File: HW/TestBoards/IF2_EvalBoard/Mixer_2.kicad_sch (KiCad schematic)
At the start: 23 parts, among them IC1 SIM-14+, IC2 LEE2-6+, IC3 LEE2-6+, J1 Conn_01x04, J2 SMA, J3 SMA, J4 SMA, J5 MS-156C3_20_, U1 B39871B4316P810

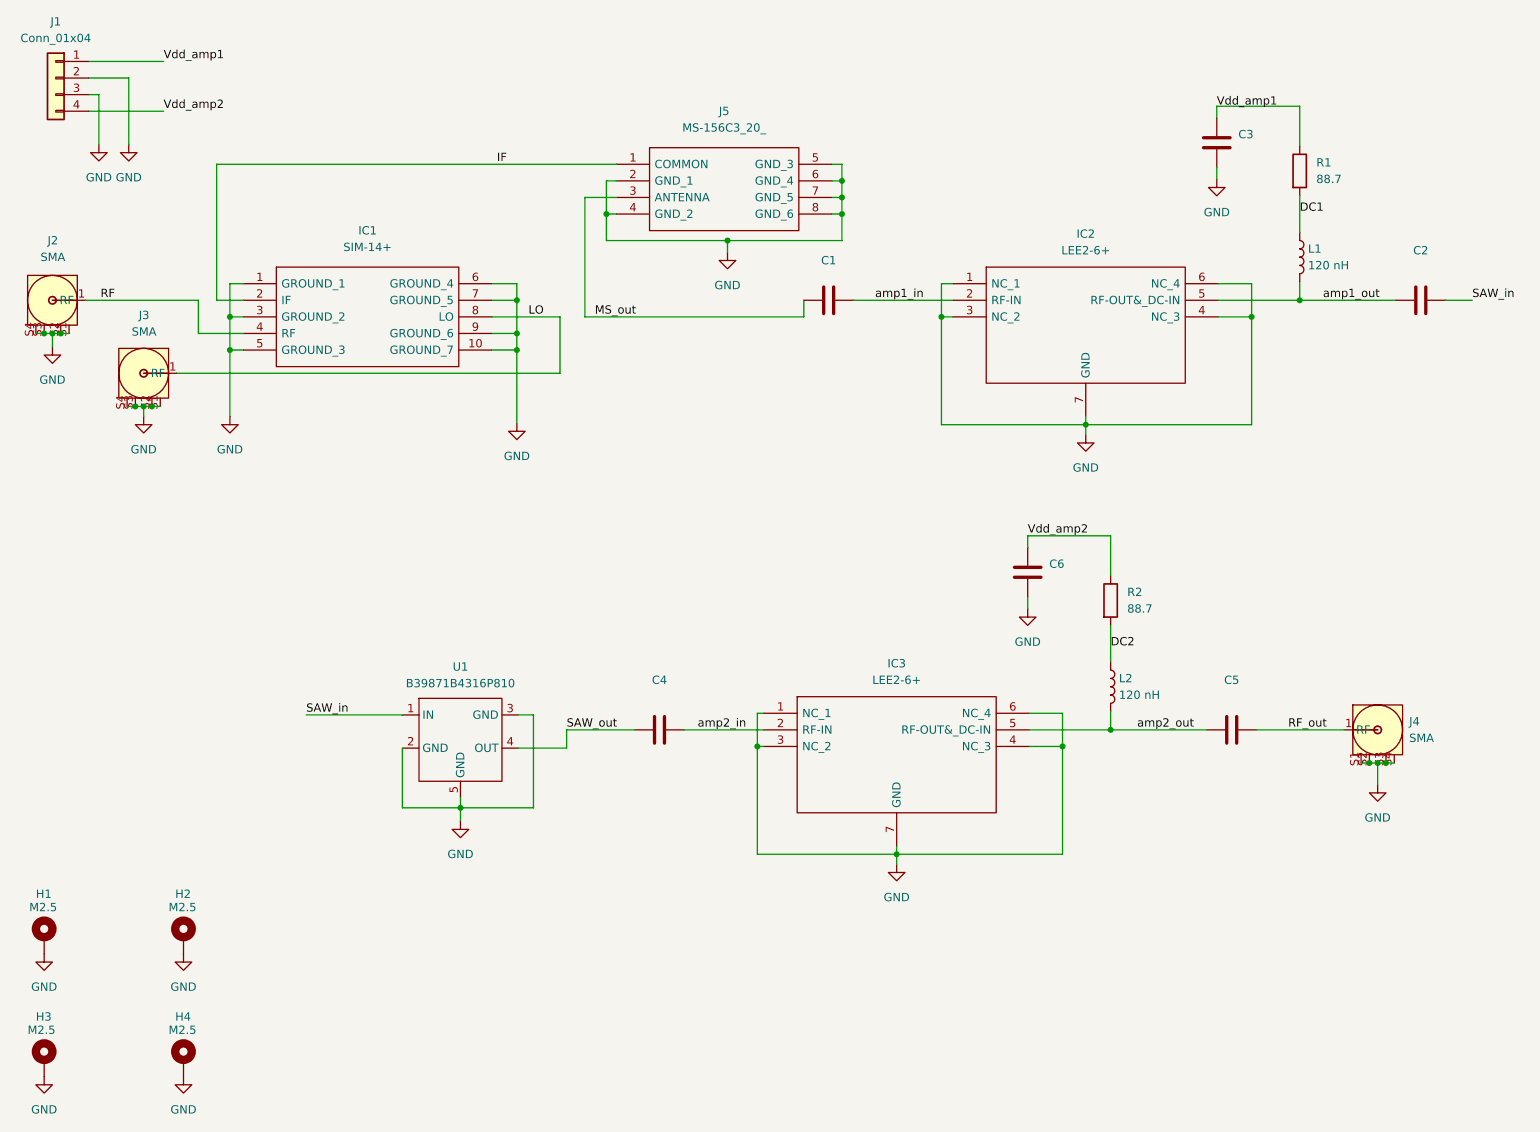
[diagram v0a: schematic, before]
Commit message: Added Evaluation Boards for RO4003C 1.52 mm
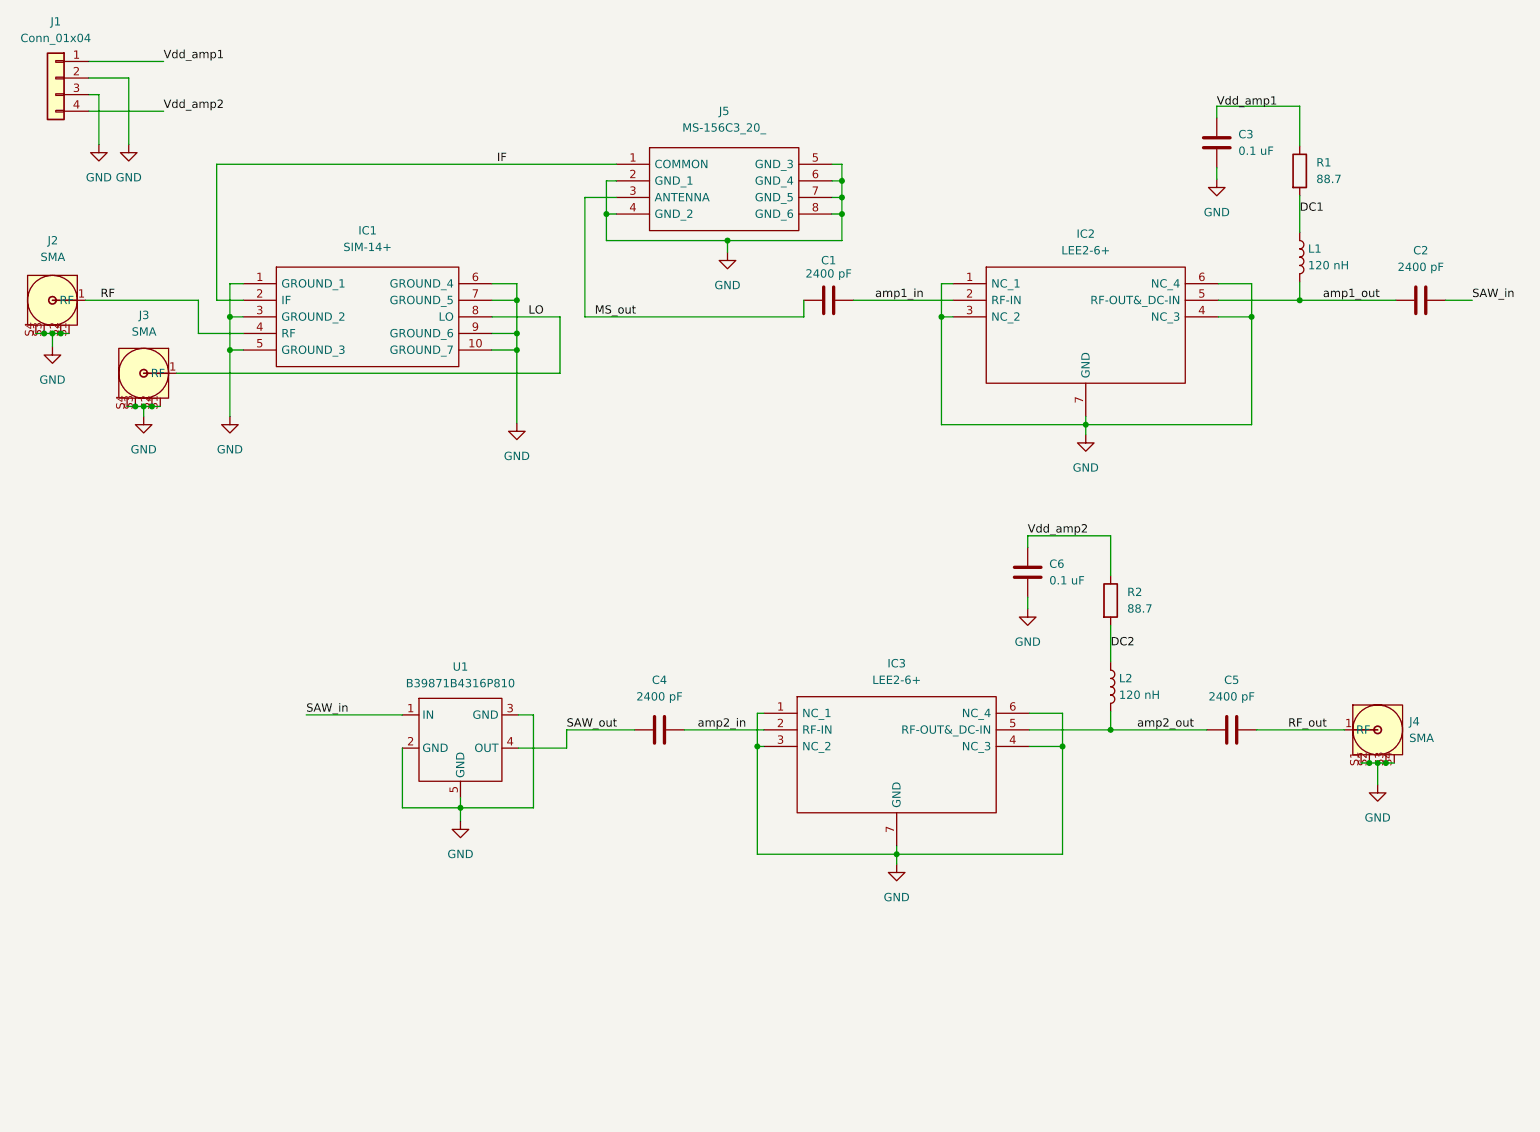
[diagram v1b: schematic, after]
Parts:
- removed H1, H2, H3, H4: M2.5, MountingHole:MountingHole_2.5mm_Pad, symbol Mechanical:MountingHole_Pad
- C1, C2, C4, C5: value (none) -> 2400 pF; footprint (none) -> Capacitor_SMD:C_0603_1608Metric_Pad1.08x0.95mm_HandSolder
- C3, C6: value (none) -> 0.1 uF; footprint (none) -> Capacitor_SMD:C_0603_1608Metric_Pad1.08x0.95mm_HandSolder
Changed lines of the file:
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@@
-    (pin "1")
-  )
-  (symbol (lib_id "Mechanical:MountingHole_Pad") (at 26.416 182.118 0) (unit 1)
-    (in_bom yes) (on_board yes)
-    (property "Reference" "H3" (id 0) (at 25.146 175.514 0)
-      (effects (font (size 1.27 1.27)) (justify left))
-    )
-    (property "Value" "M2.5" (id 1) (at 23.876 177.546 0)
-      (effects (font (size 1.27 1.27)) (justify left))
-    )
-    (property "Footprint" "MountingHole:MountingHole_2.5mm_Pad" (id 2) (at 26.416 182.118 0)
-      (effects (font (size 1.27 1.27)) hide)
-    )
-    (property "Datasheet" "~" (id 3) (at 26.416 182.118 0)
-      (effects (font (size 1.27 1.27)) hide)
-    )
     (pin "1")
   )
@@
     (in_bom yes) (on_board yes) (fields_autoplaced)
     (property "Reference" "C2" (id 0) (at 237.236 58.166 90))
-    (property "Value" "" (id 1) (at 237.236 60.706 90))
-    (property "Footprint" "" (id 2) (at 241.046 64.8208 0)
+    (property "Value" "2400 pF" (id 1) (at 237.236 60.706 90))
+    (property "Footprint" "Capacitor_SMD:C_0603_1608Metric_Pad1.08x0.95mm_HandSolder" (id 2) (at 241.046 64.8208 0)
       (effects (font (size 1.27 1.27)) hide)
     )
@@
     (in_bom yes) (on_board yes)
     (property "Reference" "C1" (id 0) (at 146.558 59.69 90))
-    (property "Value" "" (id 1) (at 146.558 61.722 90))
-    (property "Footprint" "" (id 2) (at 150.368 64.8208 0)
+    (property "Value" "2400 pF" (id 1) (at 146.558 61.722 90))
+    (property "Footprint" "Capacitor_SMD:C_0603_1608Metric_Pad1.08x0.95mm_HandSolder" (id 2) (at 150.368 64.8208 0)
       (effects (font (size 1.27 1.27)) hide)
     )
@@
     (pin "1")
     (pin "2")
-  )
-  (symbol (lib_id "Mechanical:MountingHole_Pad") (at 26.416 163.322 0) (unit 1)
-    (in_bom yes) (on_board yes)
-    (property "Reference" "H1" (id 0) (at 25.146 156.718 0)
-      (effects (font (size 1.27 1.27)) (justify left))
-    )
-    (property "Value" "M2.5" (id 1) (at 24.13 158.75 0)
-      (effects (font (size 1.27 1.27)) (justify left))
-    )
-    (property "Footprint" "MountingHole:MountingHole_2.5mm_Pad" (id 2) (at 26.416 163.322 0)
-      (effects (font (size 1.27 1.27)) hide)
-    )
-    (property "Datasheet" "~" (id 3) (at 26.416 163.322 0)
-      (effects (font (size 1.27 1.27)) hide)
-    )
-    (pin "1")
-  )
-  (symbol (lib_id "power:GND") (at 26.416 184.658 0) (unit 1)
-    (in_bom yes) (on_board yes) (fields_autoplaced)
-    (property "Reference" "#PWR0114" (id 0) (at 26.416 191.008 0)
-      (effects (font (size 1.27 1.27)) hide)
-    )
-    (property "Value" "GND" (id 1) (at 26.416 189.738 0))
-    (property "Footprint" "" (id 2) (at 26.416 184.658 0)
-      (effects (font (size 1.27 1.27)) hide)
-    )
-    (property "Datasheet" "" (id 3) (at 26.416 184.658 0)
-      (effects (font (size 1.27 1.27)) hide)
-    )
-    (pin "1")
-  )
-  (symbol (lib_id "power:GND") (at 47.752 184.658 0) (unit 1)
-    (in_bom yes) (on_board yes) (fields_autoplaced)
-    (property "Reference" "#PWR0115" (id 0) (at 47.752 191.008 0)
-      (effects (font (size 1.27 1.27)) hide)
-    )
-    (property "Value" "GND" (id 1) (at 47.752 189.738 0))
-    (property "Footprint" "" (id 2) (at 47.752 184.658 0)
-      (effects (font (size 1.27 1.27)) hide)
-    )
-    (property "Datasheet" "" (id 3) (at 47.752 184.658 0)
-      (effects (font (size 1.27 1.27)) hide)
-    )
-    (pin "1")
   )
   (symbol (lib_id "power:GND") (at 230.632 139.954 0) (unit 1)
@@
     (in_bom yes) (on_board yes) (fields_autoplaced)
     (property "Reference" "C4" (id 0) (at 120.65 123.952 90))
-    (property "Value" "" (id 1) (at 120.65 126.492 90))
-    (property "Footprint" "" (id 2) (at 124.46 130.6068 0)
+    (property "Value" "2400 pF" (id 1) (at 120.65 126.492 90))
+    (property "Footprint" "Capacitor_SMD:C_0603_1608Metric_Pad1.08x0.95mm_HandSolder" (id 2) (at 124.46 130.6068 0)
       (effects (font (size 1.27 1.27)) hide)
     )
@@
     (in_bom yes) (on_board yes) (fields_autoplaced)
     (property "Reference" "C5" (id 0) (at 208.28 123.952 90))
-    (property "Value" "" (id 1) (at 208.28 126.492 90))
-    (property "Footprint" "" (id 2) (at 212.09 130.6068 0)
+    (property "Value" "2400 pF" (id 1) (at 208.28 126.492 90))
+    (property "Footprint" "Capacitor_SMD:C_0603_1608Metric_Pad1.08x0.95mm_HandSolder" (id 2) (at 212.09 130.6068 0)
       (effects (font (size 1.27 1.27)) hide)
     )
@@
     (pin "1")
   )
-  (symbol (lib_id "power:GND") (at 47.752 165.862 0) (unit 1)
-    (in_bom yes) (on_board yes) (fields_autoplaced)
-    (property "Reference" "#PWR0113" (id 0) (at 47.752 172.212 0)
-      (effects (font (size 1.27 1.27)) hide)
-    )
-    (property "Value" "GND" (id 1) (at 47.752 170.942 0))
-    (property "Footprint" "" (id 2) (at 47.752 165.862 0)
-      (effects (font (size 1.27 1.27)) hide)
-    )
-    (property "Datasheet" "" (id 3) (at 47.752 165.862 0)
-      (effects (font (size 1.27 1.27)) hide)
-    )
-    (pin "1")
-  )
   (symbol (lib_id "Device:C") (at 205.994 41.656 180) (unit 1)
     (in_bom yes) (on_board yes) (fields_autoplaced)
@@
       (effects (font (size 1.27 1.27)) (justify right))
     )
-    (property "Value" "" (id 1) (at 209.296 42.9259 0)
+    (property "Value" "0.1 uF" (id 1) (at 209.296 42.9259 0)
       (effects (font (size 1.27 1.27)) (justify right))
     )
-    (property "Footprint" "" (id 2) (at 205.0288 37.846 0)
+    (property "Footprint" "Capacitor_SMD:C_0603_1608Metric_Pad1.08x0.95mm_HandSolder" (id 2) (at 205.0288 37.846 0)
       (effects (font (size 1.27 1.27)) hide)
     )
@@
       (effects (font (size 1.27 1.27)) (justify right))
     )
-    (property "Value" "" (id 1) (at 180.34 108.7119 0)
+    (property "Value" "0.1 uF" (id 1) (at 180.34 108.7119 0)
       (effects (font (size 1.27 1.27)) (justify right))
     )
-    (property "Footprint" "" (id 2) (at 176.0728 103.632 0)
+    (property "Footprint" "Capacitor_SMD:C_0603_1608Metric_Pad1.08x0.95mm_HandSolder" (id 2) (at 176.0728 103.632 0)
       (effects (font (size 1.27 1.27)) hide)
     )
@@
     )
     (property "Datasheet" "" (id 3) (at 185.928 86.36 0)
-      (effects (font (size 1.27 1.27)) hide)
-    )
-    (pin "1")
-  )
-  (symbol (lib_id "Mechanical:MountingHole_Pad") (at 47.752 182.118 0) (unit 1)
-    (in_bom yes) (on_board yes)
-    (property "Reference" "H4" (id 0) (at 46.482 175.514 0)
-      (effects (font (size 1.27 1.27)) (justify left))
-    )
-    (property "Value" "M2.5" (id 1) (at 45.466 177.546 0)
-      (effects (font (size 1.27 1.27)) (justify left))
-    )
-    (property "Footprint" "MountingHole:MountingHole_2.5mm_Pad" (id 2) (at 47.752 182.118 0)
-      (effects (font (size 1.27 1.27)) hide)
-    )
-    (property "Datasheet" "~" (id 3) (at 47.752 182.118 0)
       (effects (font (size 1.27 1.27)) hide)
     )
@@
     (pin "4")
   )
-  (symbol (lib_id "Mechanical:MountingHole_Pad") (at 47.752 163.322 0) (unit 1)
-    (in_bom yes) (on_board yes)
-    (property "Reference" "H2" (id 0) (at 46.482 156.718 0)
-      (effects (font (size 1.27 1.27)) (justify left))
-    )
-    (property "Value" "M2.5" (id 1) (at 45.466 158.75 0)
-      (effects (font (size 1.27 1.27)) (justify left))
-    )
-    (property "Footprint" "MountingHole:MountingHole_2.5mm_Pad" (id 2) (at 47.752 163.322 0)
-      (effects (font (size 1.27 1.27)) hide)
-    )
-    (property "Datasheet" "~" (id 3) (at 47.752 163.322 0)
-      (effects (font (size 1.27 1.27)) hide)
-    )
-    (pin "1")
-  )
   (symbol (lib_id "power:GND") (at 98.806 84.582 0) (unit 1)
     (in_bom yes) (on_board yes) (fields_autoplaced)
@@
     )
     (property "Datasheet" "" (id 3) (at 27.686 72.898 0)
-      (effects (font (size 1.27 1.27)) hide)
-    )
-    (pin "1")
-  )
-  (symbol (lib_id "power:GND") (at 26.416 165.862 0) (unit 1)
-    (in_bom yes) (on_board yes) (fields_autoplaced)
-    (property "Reference" "#PWR0112" (id 0) (at 26.416 172.212 0)
-      (effects (font (size 1.27 1.27)) hide)
-    )
-    (property "Value" "GND" (id 1) (at 26.416 170.942 0))
-    (property "Footprint" "" (id 2) (at 26.416 165.862 0)
-      (effects (font (size 1.27 1.27)) hide)
-    )
-    (property "Datasheet" "" (id 3) (at 26.416 165.862 0)
       (effects (font (size 1.27 1.27)) hide)
     )
@@
       (reference "#PWR0111") (unit 1) (value "GND") (footprint "")
     )
-    (path "/e7e652b5-53a7-4b24-aa34-a971c9dc293d"
-      (reference "#PWR0112") (unit 1) (value "GND") (footprint "")
-    )
-    (path "/a5687a11-e615-4d39-900d-98c8dc0a72a8"
-      (reference "#PWR0113") (unit 1) (value "GND") (footprint "")
-    )
-    (path "/7eedfc47-4ff2-4961-8678-7bdccf1061d6"
-      (reference "#PWR0114") (unit 1) (value "GND") (footprint "")
-    )
-    (path "/8a8db4da-2fab-4e4c-8b58-9700033bfb1e"
-      (reference "#PWR0115") (unit 1) (value "GND") (footprint "")
-    )
     (path "/ead73b10-597e-4d4e-85be-bfb0910f86fb"
       (reference "#PWR0116") (unit 1) (value "GND") (footprint "")
@@
       (reference "C6") (unit 1) (value "0.1 uF") (footprint "Capacitor_SMD:C_0603_1608Metric_Pad1.08x0.95mm_HandSolder")
     )
-    (path "/7c552e66-37eb-4e86-b6a9-7480964e261d"
-      (reference "H1") (unit 1) (value "M2.5") (footprint "MountingHole:MountingHole_2.5mm_Pad")
-    )
-    (path "/e0f7516d-8e8f-442c-8d5a-007445086b97"
-      (reference "H2") (unit 1) (value "M2.5") (footprint "MountingHole:MountingHole_2.5mm_Pad")
-    )
-    (path "/435cb3db-b52c-4fca-bb93-45f5cd7c0781"
-      (reference "H3") (unit 1) (value "M2.5") (footprint "MountingHole:MountingHole_2.5mm_Pad")
-    )
-    (path "/c19e2542-60a9-4175-9949-2abf370eb6e5"
-      (reference "H4") (unit 1) (value "M2.5") (footprint "MountingHole:MountingHole_2.5mm_Pad")
-    )
     (path "/c2eb7556-7c6b-4d8d-8a3c-6deaae016b87"
